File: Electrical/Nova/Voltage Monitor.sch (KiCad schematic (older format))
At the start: 3 parts, among them U1 OP179GRT

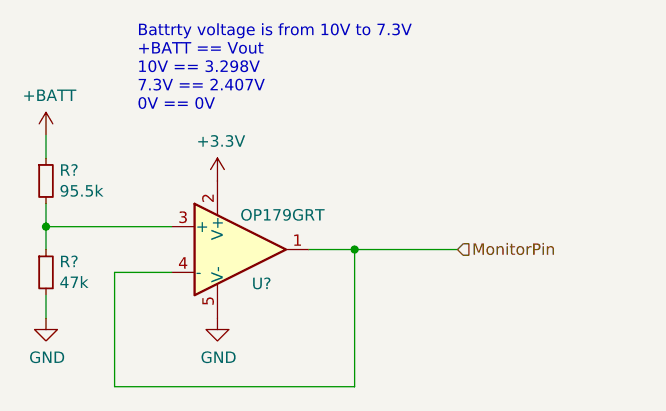
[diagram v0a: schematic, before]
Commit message: Fixed some more footprints
still a little weird but good for the 26th
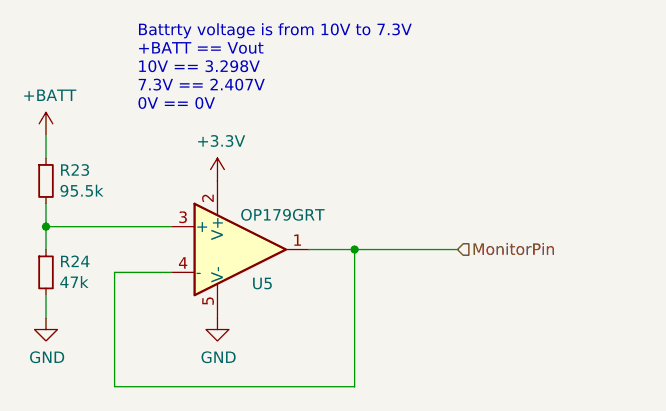
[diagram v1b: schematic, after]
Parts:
- R23, R24: renamed from R?; footprint (none) -> Resistor_SMD:R_0603_1608Metric
- renumbered U1 to U5
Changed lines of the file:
@@
 $EndDescr
 $Comp
-L Amplifier_Operational:OP179GRT U1
+L Amplifier_Operational:OP179GRT U5
 U 1 1 5F935857
 P 5700 3900
-F 0 "U?" H 5750 3750 50  0000 L CNN
+F 0 "U5" H 5750 3750 50  0000 L CNN
 F 1 "OP179GRT" H 5700 4050 50  0000 L CNN
 F 2 "Package_TO_SOT_SMD:SOT-23-5" H 5700 3900 50  0001 C CNN
@@
 $EndComp
 $Comp
-L power:+BATT #PWR?
+L power:+BATT #PWR0111
 U 1 1 5F93B73B
 P 4850 3400
-F 0 "#PWR?" H 4850 3250 50  0001 C CNN
+F 0 "#PWR0111" H 4850 3250 50  0001 C CNN
 F 1 "+BATT" H 4865 3573 50  0000 C CNN
 F 2 "" H 4850 3400 50  0001 C CNN
@@
 $EndComp
 $Comp
-L power:GND #PWR?
+L power:GND #PWR0112
 U 1 1 5F93C2F4
 P 5600 4200
-F 0 "#PWR?" H 5600 3950 50  0001 C CNN
+F 0 "#PWR0112" H 5600 3950 50  0001 C CNN
 F 1 "GND" H 5605 4027 50  0000 C CNN
 F 2 "" H 5600 4200 50  0001 C CNN
@@
 $EndComp
 $Comp
-L Device:R_Small R?
+L Device:R_Small R23
 U 1 1 5F93E280
 P 4850 3600
-F 0 "R?" H 4909 3646 50  0000 L CNN
+F 0 "R23" H 4909 3646 50  0000 L CNN
 F 1 "95.5k" H 4909 3555 50  0000 L CNN
-F 2 "" H 4850 3600 50  0001 C CNN
+F 2 "Resistor_SMD:R_0603_1608Metric" H 4850 3600 50  0001 C CNN
 F 3 "~" H 4850 3600 50  0001 C CNN
 	1    4850 3600
@@
 $EndComp
 $Comp
-L Device:R_Small R?
+L Device:R_Small R24
 U 1 1 5F93F1CB
 P 4850 4000
-F 0 "R?" H 4909 4046 50  0000 L CNN
+F 0 "R24" H 4909 4046 50  0000 L CNN
 F 1 "47k" H 4909 3955 50  0000 L CNN
-F 2 "" H 4850 4000 50  0001 C CNN
+F 2 "Resistor_SMD:R_0603_1608Metric" H 4850 4000 50  0001 C CNN
 F 3 "~" H 4850 4000 50  0001 C CNN
 	1    4850 4000
@@
 	6200 4500 5150 4500
 $Comp
-L power:+3.3V #PWR?
+L power:+3.3V #PWR0113
 U 1 1 5F94E8D1
 P 5600 3600
-F 0 "#PWR?" H 5600 3450 50  0001 C CNN
+F 0 "#PWR0113" H 5600 3450 50  0001 C CNN
 F 1 "+3.3V" H 5615 3773 50  0000 C CNN
 F 2 "" H 5600 3600 50  0001 C CNN
@@
 $EndComp
 $Comp
-L power:GND #PWR?
+L power:GND #PWR0114
 U 1 1 5F94FFAB
 P 4850 4200
-F 0 "#PWR?" H 4850 3950 50  0001 C CNN
+F 0 "#PWR0114" H 4850 3950 50  0001 C CNN
 F 1 "GND" H 4855 4027 50  0000 C CNN
 F 2 "" H 4850 4200 50  0001 C CNN

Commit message: Electrical REV1
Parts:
- R23, R24: footprint Resistor_SMD:R_0603_1608Metric -> Resistor_SMD:R_0603_1608Metric_Pad1.05x0.95mm_HandSolder
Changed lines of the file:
@@
 $Descr A4 11693 8268
 encoding utf-8
-Sheet 22 22
+Sheet 19 22
 Title ""
 Date ""
@@
 F 0 "R23" H 4909 3646 50  0000 L CNN
 F 1 "95.5k" H 4909 3555 50  0000 L CNN
-F 2 "Resistor_SMD:R_0603_1608Metric" H 4850 3600 50  0001 C CNN
+F 2 "Resistor_SMD:R_0603_1608Metric_Pad1.05x0.95mm_HandSolder" H 4850 3600 50  0001 C CNN
 F 3 "~" H 4850 3600 50  0001 C CNN
 	1    4850 3600
@@
 F 0 "R24" H 4909 4046 50  0000 L CNN
 F 1 "47k" H 4909 3955 50  0000 L CNN
-F 2 "Resistor_SMD:R_0603_1608Metric" H 4850 4000 50  0001 C CNN
+F 2 "Resistor_SMD:R_0603_1608Metric_Pad1.05x0.95mm_HandSolder" H 4850 4000 50  0001 C CNN
 F 3 "~" H 4850 4000 50  0001 C CNN
 	1    4850 4000

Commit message: Removed Obsolete Components & Modified Format  and Misc
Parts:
- R23, R24: footprint Resistor_SMD:R_0603_1608Metric_Pad1.05x0.95mm_HandSolder -> Resistor_SMD:R_0402_1005Metric
- U5: footprint Package_TO_SOT_SMD:SOT-23-5 -> (none)
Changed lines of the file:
@@
 $Descr A4 11693 8268
 encoding utf-8
-Sheet 19 21
+Sheet 15 19
 Title ""
 Date ""
@@
 F 0 "U5" H 5750 3750 50  0000 L CNN
 F 1 "OP179GRT" H 5700 4050 50  0000 L CNN
-F 2 "Package_TO_SOT_SMD:SOT-23-5" H 5700 3900 50  0001 C CNN
+F 2 "" H 5700 3900 50  0001 C CNN
 F 3 "https://www.analog.com/media/en/technical-documentation/data-sheets/OP179_279.pdf" H 5700 4100 50  0001 C CNN
 	1    5700 3900
@@
 F 0 "R23" H 4909 3646 50  0000 L CNN
 F 1 "95.5k" H 4909 3555 50  0000 L CNN
-F 2 "Resistor_SMD:R_0603_1608Metric_Pad1.05x0.95mm_HandSolder" H 4850 3600 50  0001 C CNN
+F 2 "Resistor_SMD:R_0402_1005Metric" H 4850 3600 50  0001 C CNN
 F 3 "~" H 4850 3600 50  0001 C CNN
 	1    4850 3600
@@
 F 0 "R24" H 4909 4046 50  0000 L CNN
 F 1 "47k" H 4909 3955 50  0000 L CNN
-F 2 "Resistor_SMD:R_0603_1608Metric_Pad1.05x0.95mm_HandSolder" H 4850 4000 50  0001 C CNN
+F 2 "Resistor_SMD:R_0402_1005Metric" H 4850 4000 50  0001 C CNN
 F 3 "~" H 4850 4000 50  0001 C CNN
 	1    4850 4000

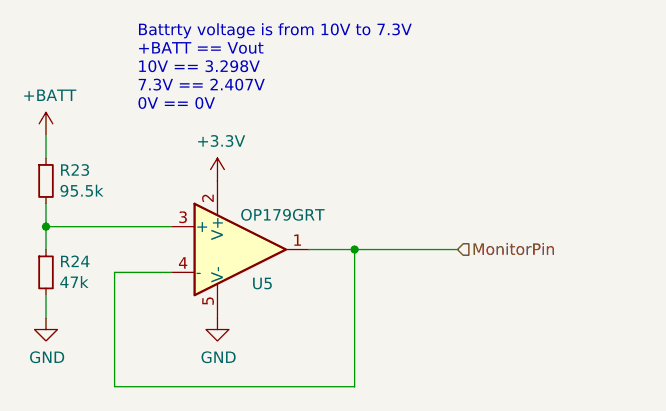
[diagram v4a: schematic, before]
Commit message: Added New Components and Cleaned up A lot of Schematics/Properties
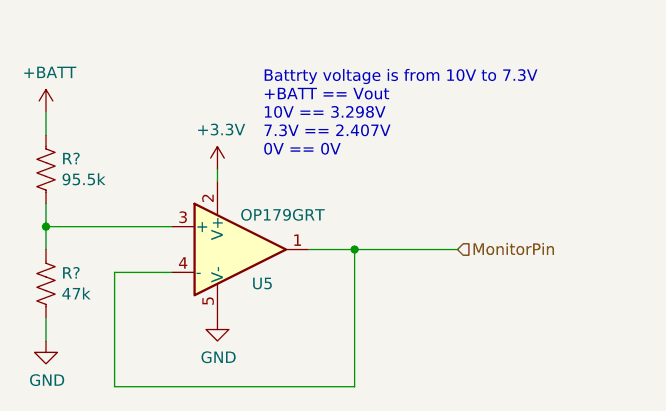
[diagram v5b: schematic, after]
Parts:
- removed R23: 95.5k, Resistor_SMD:R_0402_1005Metric, symbol Device:R_Small
- removed R24: 47k, Resistor_SMD:R_0402_1005Metric, symbol Device:R_Small
- added R?: 95.5k, symbol Device:R_US
- added R?: 47k, symbol Device:R_US
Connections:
- net +BATT: now also R?.1
- net GND: now also R?.2
- net at U5.3 (+): now also R?.1, R?.2
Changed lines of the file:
@@
 $Descr A4 11693 8268
 encoding utf-8
-Sheet 15 19
+Sheet 10 20
 Title ""
 Date ""
@@
 L power:+BATT #PWR0111
 U 1 1 5F93B73B
-P 4850 3400
-F 0 "#PWR0111" H 4850 3250 50  0001 C CNN
-F 1 "+BATT" H 4865 3573 50  0000 C CNN
-F 2 "" H 4850 3400 50  0001 C CNN
-F 3 "" H 4850 3400 50  0001 C CNN
-	1    4850 3400
+P 4850 3300
+F 0 "#PWR0111" H 4850 3150 50  0001 C CNN
+F 1 "+BATT" H 4865 3473 50  0000 C CNN
+F 2 "" H 4850 3300 50  0001 C CNN
+F 3 "" H 4850 3300 50  0001 C CNN
+	1    4850 3300
 	1    0    0    -1
 $EndComp
@@
 	1    0    0    -1
 $EndComp
-$Comp
-L Device:R_Small R23
-U 1 1 5F93E280
-P 4850 3600
-F 0 "R23" H 4909 3646 50  0000 L CNN
-F 1 "95.5k" H 4909 3555 50  0000 L CNN
-F 2 "Resistor_SMD:R_0402_1005Metric" H 4850 3600 50  0001 C CNN
-F 3 "~" H 4850 3600 50  0001 C CNN
-	1    4850 3600
-	1    0    0    -1
-$EndComp
-$Comp
-L Device:R_Small R24
-U 1 1 5F93F1CB
-P 4850 4000
-F 0 "R24" H 4909 4046 50  0000 L CNN
-F 1 "47k" H 4909 3955 50  0000 L CNN
-F 2 "Resistor_SMD:R_0402_1005Metric" H 4850 4000 50  0001 C CNN
-F 3 "~" H 4850 4000 50  0001 C CNN
-	1    4850 4000
-	1    0    0    -1
-$EndComp
 Wire Wire Line
-	4850 3400 4850 3500
+	4850 3300 4850 3400
 Wire Wire Line
 	4850 3700 4850 3800
 Wire Wire Line
-	4850 4100 4850 4200
+	4850 4200 4850 4300
 Connection ~ 4850 3800
 Wire Wire Line
@@
 L power:+3.3V #PWR0113
 U 1 1 5F94E8D1
-P 5600 3600
-F 0 "#PWR0113" H 5600 3450 50  0001 C CNN
-F 1 "+3.3V" H 5615 3773 50  0000 C CNN
-F 2 "" H 5600 3600 50  0001 C CNN
-F 3 "" H 5600 3600 50  0001 C CNN
-	1    5600 3600
+P 5600 3550
+F 0 "#PWR0113" H 5600 3400 50  0001 C CNN
+F 1 "+3.3V" H 5615 3723 50  0000 C CNN
+F 2 "" H 5600 3550 50  0001 C CNN
+F 3 "" H 5600 3550 50  0001 C CNN
+	1    5600 3550
 	1    0    0    -1
 $EndComp
@@
 L power:GND #PWR0114
 U 1 1 5F94FFAB
-P 4850 4200
-F 0 "#PWR0114" H 4850 3950 50  0001 C CNN
-F 1 "GND" H 4855 4027 50  0000 C CNN
-F 2 "" H 4850 4200 50  0001 C CNN
-F 3 "" H 4850 4200 50  0001 C CNN
-	1    4850 4200
+P 4850 4300
+F 0 "#PWR0114" H 4850 4050 50  0001 C CNN
+F 1 "GND" H 4855 4127 50  0000 C CNN
+F 2 "" H 4850 4300 50  0001 C CNN
+F 3 "" H 4850 4300 50  0001 C CNN
+	1    4850 4300
 	1    0    0    -1
 $EndComp
@@
 Wire Wire Line
 	5150 4000 5150 4500
-Text Notes 5250 3300 0    50   ~ 0
+Text Notes 5800 3500 0    50   ~ 0
 Battrty voltage is from 10V to 7.3V\n+BATT == Vout\n10V == 3.298V\n7.3V == 2.407V\n0V == 0V
 Text HLabel 6650 3900 2    50   Input ~ 0
 MonitorPin
+$Comp
+L Device:R_US R?
+U 1 1 6024316E
+P 4850 3550
+F 0 "R?" H 4918 3596 50  0000 L CNN
+F 1 "95.5k" H 4918 3505 50  0000 L CNN
+F 2 "" V 4890 3540 50  0001 C CNN
+F 3 "~" H 4850 3550 50  0001 C CNN
+	1    4850 3550
+	1    0    0    -1
+$EndComp
+$Comp
+L Device:R_US R?
+U 1 1 60243E65
+P 4850 4050
+F 0 "R?" H 4918 4096 50  0000 L CNN
+F 1 "47k" H 4918 4005 50  0000 L CNN
+F 2 "" V 4890 4040 50  0001 C CNN
+F 3 "~" H 4850 4050 50  0001 C CNN
+	1    4850 4050
+	1    0    0    -1
+$EndComp
+Wire Wire Line
+	5600 3600 5600 3550
 $EndSCHEMATC

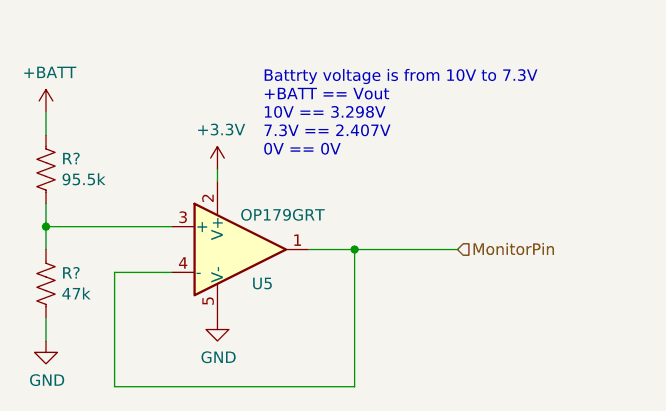
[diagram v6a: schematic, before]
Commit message: More Pin Additions for connectors and other misc.
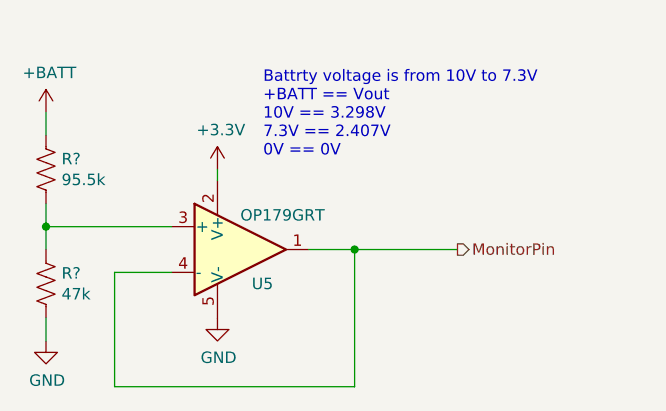
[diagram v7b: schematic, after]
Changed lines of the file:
@@
 $Descr A4 11693 8268
 encoding utf-8
-Sheet 10 21
+Sheet 9 21
 Title ""
 Date ""
@@
 Text Notes 5800 3500 0    50   ~ 0
 Battrty voltage is from 10V to 7.3V\n+BATT == Vout\n10V == 3.298V\n7.3V == 2.407V\n0V == 0V
-Text HLabel 6650 3900 2    50   Input ~ 0
+Text HLabel 6650 3900 2    50   Output ~ 0
 MonitorPin
 $Comp

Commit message: Added a bunch of footprints to symbols
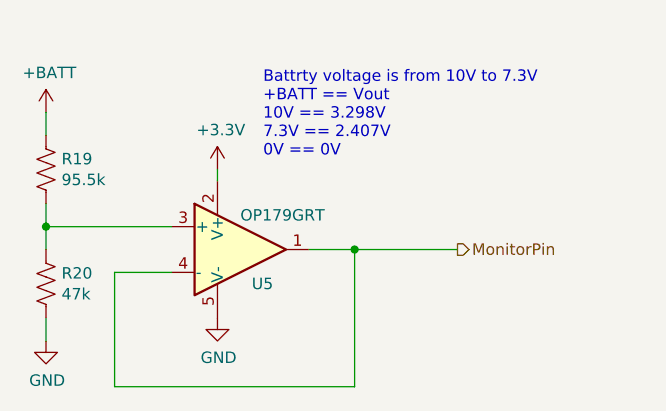
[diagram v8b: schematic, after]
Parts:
- R19, R20: renamed from R?; footprint (none) -> Resistor_SMD:R_0402_1005Metric
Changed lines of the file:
@@
 MonitorPin
 $Comp
-L Device:R_US R?
+L Device:R_US R19
 U 1 1 6024316E
 P 4850 3550
-F 0 "R?" H 4918 3596 50  0000 L CNN
+F 0 "R19" H 4918 3596 50  0000 L CNN
 F 1 "95.5k" H 4918 3505 50  0000 L CNN
-F 2 "" V 4890 3540 50  0001 C CNN
+F 2 "Resistor_SMD:R_0402_1005Metric" V 4890 3540 50  0001 C CNN
 F 3 "~" H 4850 3550 50  0001 C CNN
 	1    4850 3550
@@
 $EndComp
 $Comp
-L Device:R_US R?
+L Device:R_US R20
 U 1 1 60243E65
 P 4850 4050
-F 0 "R?" H 4918 4096 50  0000 L CNN
+F 0 "R20" H 4918 4096 50  0000 L CNN
 F 1 "47k" H 4918 4005 50  0000 L CNN
-F 2 "" V 4890 4040 50  0001 C CNN
+F 2 "Resistor_SMD:R_0402_1005Metric" V 4890 4040 50  0001 C CNN
 F 3 "~" H 4850 4050 50  0001 C CNN
 	1    4850 4050
